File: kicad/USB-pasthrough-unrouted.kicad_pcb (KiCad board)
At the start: 4 copper layers, 40 x 100 mm, 93 parts, among them J1 USB_Power, J10 MicroSD, J4 Power_Sel, J5 SPI Display, J6 SWD, J7 Cortex Debug, J8 USB_C, J9 USB_A, SW1 Boot0, SW2 Reset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

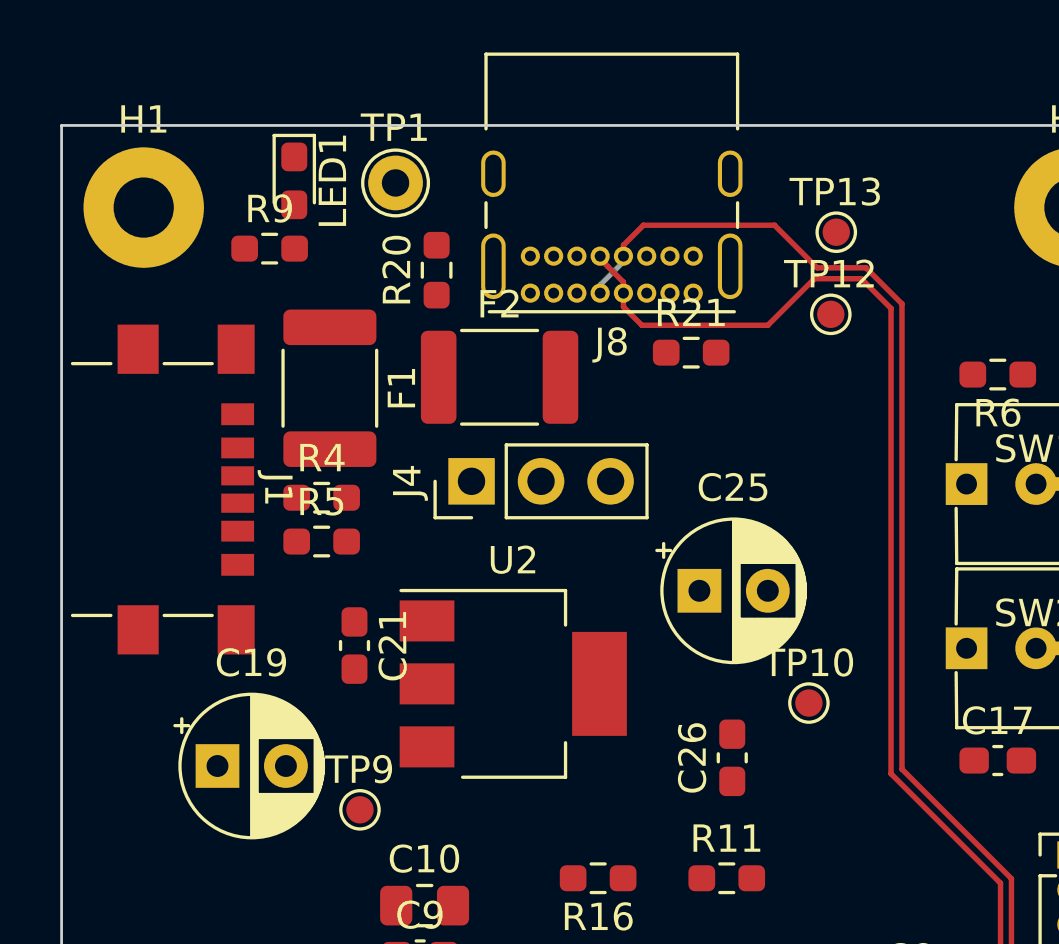
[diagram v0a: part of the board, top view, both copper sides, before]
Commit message: Generate clean unrouted PCB
1. place components
2. manually route USB differential signals
3. manually route Power Supply
4. connect 3V3 and GND to energize power planes
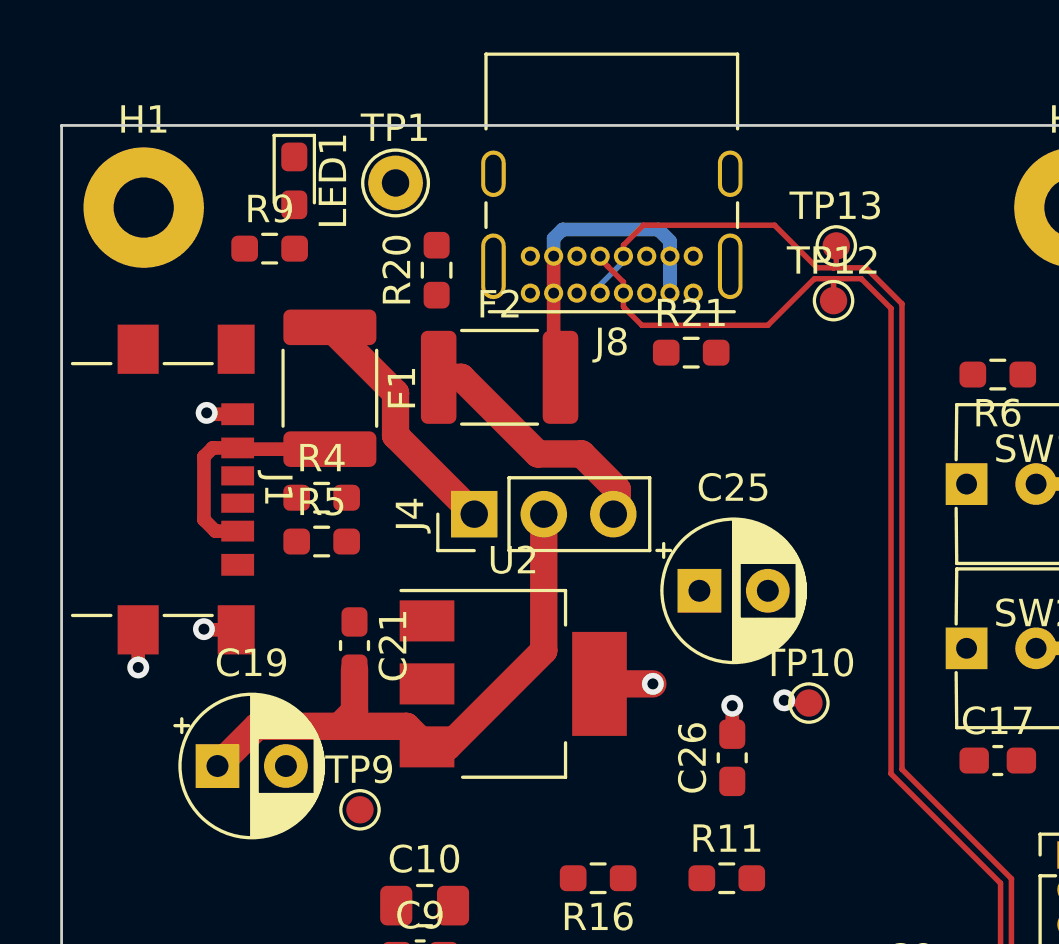
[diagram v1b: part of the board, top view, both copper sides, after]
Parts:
- moved J4 1.20 mm to (115.1, 64.2)
- moved TP12 0.51 mm to (128.2, 56.4)
- moved TP13 0.50 mm to (128.3, 54.4)
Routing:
- net +5V: track 0.00 -> 21.6 mm
- net Net-(F2-Pad2): track 0.00 -> 11.6 mm
- net /VBUS_DATA: track 0.00 -> 9.18 mm
- net /VBUS_PWR: track 0.00 -> 9.01 mm
- net Net-(F1-Pad2): track 0.00 -> 8.46 mm
- net +3V3: track 0.00 -> 3.93 mm, vias 0 -> 3
- net GND: track 0.00 -> 3.72 mm, vias 0 -> 3
- net /USBC-: track 56.2 -> 57.0 mm
- net /USBC+: track 54.8 -> 55.7 mm
- added copper zone on In2.Cu, net +3V3
- added copper zone on In1.Cu, net GND
- removed copper zone on In1.Cu, net (none)
- removed copper zone on In2.Cu, net (none)
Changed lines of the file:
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@@
   )
   (footprint "Connector_PinHeader_2.54mm:PinHeader_1x03_P2.54mm_Vertical" (layer "F.Cu")
-    (at 114.975 63 90)
+    (at 115.075 64.2 90)
     (descr "Through hole straight pin header, 1x03, 2.54mm pitch, single row")
     (tags "Through hole pin header THT 1x03 2.54mm single row")
@@
   )
   (footprint "TestPoint:TestPoint_Pad_D1.0mm" (layer "F.Cu")
-    (at 128.1 56.9)
+    (at 128.2 56.4)
     (descr "SMD pad as test Point, diameter 1.0mm")
     (tags "test point SMD pad")
@@
   )
   (footprint "TestPoint:TestPoint_Pad_D1.0mm" (layer "F.Cu")
-    (at 128.3 53.9)
+    (at 128.3 54.4)
     (descr "SMD pad as test Point, diameter 1.0mm")
     (tags "test point SMD pad")
@@
   )
   (gr_rect (start 100 50) (end 140 150) (layer "Edge.Cuts") (width 0.1) (fill none))
+  (segment (start 126.5 71.1) (end 126.4 71) (width 0.25) (layer "F.Cu") (net 2))
+  (segment (start 119.65 70.4) (end 121.6 70.4) (width 1) (layer "F.Cu") (net 2))
+  (segment (start 124.5 72.2375) (end 124.5 71.2) (width 0.5) (layer "F.Cu") (net 2))
+  (segment (start 127.3 71.1) (end 126.5 71.1) (width 0.25) (layer "F.Cu") (net 2))
+  (via (at 126.4 71) (size 0.8) (drill 0.4) (layers "F.Cu" "B.Cu") (net 2))
+  (via (at 121.6 70.4) (size 0.8) (drill 0.4) (layers "F.Cu" "B.Cu") (net 2))
+  (via (at 124.5 71.2) (size 0.8) (drill 0.4) (layers "F.Cu" "B.Cu") (net 2))
+  (segment (start 106.4325 60.55) (end 105.35 60.55) (width 0.5) (layer "F.Cu") (net 3))
+  (segment (start 105.35 60.55) (end 105.3 60.5) (width 0.5) (layer "F.Cu") (net 3))
+  (segment (start 102.7975 69.7975) (end 102.8 69.8) (width 0.5) (layer "F.Cu") (net 3))
+  (segment (start 106.3775 68.425) (end 105.225 68.425) (width 0.5) (layer "F.Cu") (net 3))
+  (segment (start 105.225 68.425) (end 105.2 68.4) (width 0.5) (layer "F.Cu") (net 3))
+  (segment (start 102.7975 68.425) (end 102.7975 69.7975) (width 0.5) (layer "F.Cu") (net 3))
+  (via (at 102.8 69.8) (size 0.8) (drill 0.4) (layers "F.Cu" "B.Cu") (net 3))
+  (via (at 105.3 60.5) (size 0.8) (drill 0.4) (layers "F.Cu" "B.Cu") (net 3))
+  (via (at 105.2 68.4) (size 0.8) (drill 0.4) (layers "F.Cu" "B.Cu") (net 3))
+  (segment (start 117.615 69.185) (end 114.1 72.7) (width 1) (layer "F.Cu") (net 14))
+  (segment (start 107.144888 71.95) (end 105.694888 73.4) (width 1) (layer "F.Cu") (net 14))
+  (segment (start 114.1 72.7) (end 113.35 72.7) (width 1) (layer "F.Cu") (net 14))
+  (segment (start 110.7 71.4) (end 110.15 71.95) (width 1) (layer "F.Cu") (net 14))
+  (segment (start 113.35 72.7) (end 112.6 71.95) (width 1) (layer "F.Cu") (net 14))
+  (segment (start 110.15 71.95) (end 107.144888 71.95) (width 1) (layer "F.Cu") (net 14))
+  (segment (start 117.615 64.2) (end 117.615 69.185) (width 1) (layer "F.Cu") (net 14))
+  (segment (start 112.6 71.95) (end 110.15 71.95) (width 1) (layer "F.Cu") (net 14))
+  (segment (start 110.7 69.8625) (end 110.7 71.4) (width 1) (layer "F.Cu") (net 14))
+  (segment (start 115.075 64.2) (end 112.2 61.325) (width 1) (layer "F.Cu") (net 19))
+  (segment (start 112.2 61.325) (end 112.2 59.775) (width 1) (layer "F.Cu") (net 19))
+  (segment (start 112.2 59.775) (end 109.8 57.375) (width 1) (layer "F.Cu") (net 19))
+  (segment (start 105.2 64.4) (end 105.62 64.82) (width 0.5) (layer "F.Cu") (net 20))
+  (segment (start 106.4775 61.825) (end 106.4325 61.78) (width 0.5) (layer "F.Cu") (net 20))
+  (segment (start 105.52 61.78) (end 105.2 62.1) (width 0.5) (layer "F.Cu") (net 20))
+  (segment (start 109.8 61.825) (end 106.4775 61.825) (width 0.5) (layer "F.Cu") (net 20))
+  (segment (start 105.2 62.1) (end 105.2 64.4) (width 0.5) (layer "F.Cu") (net 20))
+  (segment (start 105.62 64.82) (end 106.4325 64.82) (width 0.5) (layer "F.Cu") (net 20))
+  (segment (start 106.4325 61.78) (end 105.52 61.78) (width 0.5) (layer "F.Cu") (net 20))
+  (segment (start 119 62) (end 120.3 63.3) (width 1) (layer "F.Cu") (net 21))
+  (segment (start 120.3 63.3) (end 120.3 64.055) (width 1) (layer "F.Cu") (net 21))
+  (segment (start 117.4 62) (end 119 62) (width 1) (layer "F.Cu") (net 21))
+  (segment (start 113.775 59.2) (end 114.6 59.2) (width 1) (layer "F.Cu") (net 21))
+  (segment (start 114.6 59.2) (end 117.4 62) (width 1) (layer "F.Cu") (net 21))
+  (segment (start 120.3 64.055) (end 120.155 64.2) (width 1) (layer "F.Cu") (net 21))
+  (segment (start 117.975 54.775) (end 117.975 56.125) (width 0.5) (layer "F.Cu") (net 22))
+  (segment (start 117.975 56.125) (end 117.975 58.95) (width 0.5) (layer "F.Cu") (net 22))
+  (segment (start 117.975 58.95) (end 118.225 59.2) (width 0.5) (layer "F.Cu") (net 22))
+  (segment (start 122.225 54.775) (end 122.225 56.125) (width 0.5) (layer "B.Cu") (net 22))
+  (segment (start 121.8 53.8) (end 122.225 54.225) (width 0.5) (layer "B.Cu") (net 22))
+  (segment (start 117.975 54.775) (end 117.975 54.125) (width 0.5) (layer "B.Cu") (net 22))
+  (segment (start 118.3 53.8) (end 121.8 53.8) (width 0.5) (layer "B.Cu") (net 22))
+  (segment (start 122.225 54.225) (end 122.225 54.775) (width 0.5) (layer "B.Cu") (net 22))
+  (segment (start 117.975 54.125) (end 118.3 53.8) (width 0.5) (layer "B.Cu") (net 22))
+  (segment (start 129.217156 55.6) (end 128.3 55.6) (width 0.2) (layer "F.Cu") (net 40))
   (segment (start 127.675 93) (end 127.725 93.05) (width 0.2) (layer "F.Cu") (net 40))
   (segment (start 130.3 56.682844) (end 129.217156 55.6) (width 0.2) (layer "F.Cu") (net 40))
   (segment (start 119.675 54.775) (end 119.675 54.875) (width 0.2) (layer "F.Cu") (net 40))
-  (segment (start 129.217156 55.6) (end 127.5 55.6) (width 0.2) (layer "F.Cu") (net 40))
   (segment (start 125.8 57.3) (end 121.2 57.3) (width 0.2) (layer "F.Cu") (net 40))
+  (segment (start 128.2 56.4) (end 128.2 55.7) (width 0.2) (layer "F.Cu") (net 40))
   (segment (start 127.725 93.05) (end 128.767156 93.05) (width 0.2) (layer "F.Cu") (net 40))
   (segment (start 128.767156 93.05) (end 134.3 87.517156) (width 0.2) (layer "F.Cu") (net 40))
   (segment (start 130.3 73.682844) (end 130.3 56.682844) (width 0.2) (layer "F.Cu") (net 40))
+  (segment (start 128.3 55.6) (end 127.5 55.6) (width 0.2) (layer "F.Cu") (net 40))
   (segment (start 134.3 87.517156) (end 134.3 77.682844) (width 0.2) (layer "F.Cu") (net 40))
   (segment (start 127.5 55.6) (end 125.8 57.3) (width 0.2) (layer "F.Cu") (net 40))
   (segment (start 121.2 57.3) (end 120.525 56.625) (width 0.2) (layer "F.Cu") (net 40))
+  (segment (start 128.2 55.7) (end 128.3 55.6) (width 0.2) (layer "F.Cu") (net 40))
   (segment (start 120.525 55.725) (end 120.525 56.125) (width 0.2) (layer "F.Cu") (net 40))
   (segment (start 120.525 56.625) (end 120.525 56.125) (width 0.2) (layer "F.Cu") (net 40))
@@
   (segment (start 128.932844 93.45) (end 134.7 87.682844) (width 0.2) (layer "F.Cu") (net 41))
   (segment (start 120.525 54.375) (end 120.525 54.775) (width 0.2) (layer "F.Cu") (net 41))
-  (segment (start 129.382844 55.2) (end 127.6 55.2) (width 0.2) (layer "F.Cu") (net 41))
+  (segment (start 128.2 55.2) (end 127.6 55.2) (width 0.2) (layer "F.Cu") (net 41))
+  (segment (start 128.3 54.4) (end 128.3 55.1) (width 0.2) (layer "F.Cu") (net 41))
   (segment (start 130.7 73.517156) (end 130.7 56.517156) (width 0.2) (layer "F.Cu") (net 41))
   (segment (start 130.7 56.517156) (end 129.382844 55.2) (width 0.2) (layer "F.Cu") (net 41))
   (segment (start 134.7 77.517156) (end 130.7 73.517156) (width 0.2) (layer "F.Cu") (net 41))
+  (segment (start 129.382844 55.2) (end 128.2 55.2) (width 0.2) (layer "F.Cu") (net 41))
   (segment (start 121.255 53.645) (end 120.525 54.375) (width 0.2) (layer "F.Cu") (net 41))
   (segment (start 126.045 53.645) (end 121.255 53.645) (width 0.2) (layer "F.Cu") (net 41))
@@
   (segment (start 127.725 93.45) (end 128.932844 93.45) (width 0.2) (layer "F.Cu") (net 41))
   (segment (start 127.6 55.2) (end 126.045 53.645) (width 0.2) (layer "F.Cu") (net 41))
+  (segment (start 128.3 55.1) (end 128.2 55.2) (width 0.2) (layer "F.Cu") (net 41))
   (segment (start 119.675 55.825) (end 119.675 56.125) (width 0.2) (layer "B.Cu") (net 41))
   (segment (start 120.525 54.775) (end 120.4 54.9) (width 0.2) (layer "B.Cu") (net 41))
@@
   (segment (start 125.05 88.05) (end 125.05 111.096446) (width 0.25) (layer "B.Cu") (net 46))
   (segment (start 121 139.507107) (end 121 140.8) (width 0.25) (layer "B.Cu") (net 46))
-  (zone (net 0) (net_name "") (layer "In1.Cu") (hatch edge 0.508)
+  (zone (net 3) (net_name "GND") (layer "In1.Cu") (hatch edge 0.508)
     (connect_pads yes (clearance 0.2))
     (min_thickness 0.254) (filled_areas_thickness no)
@@
     (polygon
       (pts
-        (xy 139.9 50.9)
-        (xy 140.9 50.9)
-        (xy 140.9 150)
-        (xy 100.5 150)
-        (xy 99.9 50.3)
+        (xy 140 50)
+        (xy 140 50)
+        (xy 140 150)
+        (xy 100 150)
+        (xy 100 50)
       )
     )
   )
-  (zone (net 0) (net_name "") (layer "In2.Cu") (name "Power") (hatch edge 0.508)
+  (zone (net 2) (net_name "+3V3") (layer "In2.Cu") (name "Power") (hatch edge 0.508)
     (connect_pads yes (clearance 0.2))
     (min_thickness 0.254) (filled_areas_thickness no)
@@
     (polygon
       (pts
-        (xy 140.9 50.9)
-        (xy 139.6 52.1)
-        (xy 141.2 150.3)
-        (xy 100.8 149.3)
-        (xy 99.9 50.3)
+        (xy 140 50)
+        (xy 140 50.1)
+        (xy 140 150)
+        (xy 100 150)
+        (xy 100 50)
       )
     )
